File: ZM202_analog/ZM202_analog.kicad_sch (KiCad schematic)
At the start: 11 parts, among them U1 LM324, U13 LM393B, U14 LM358B

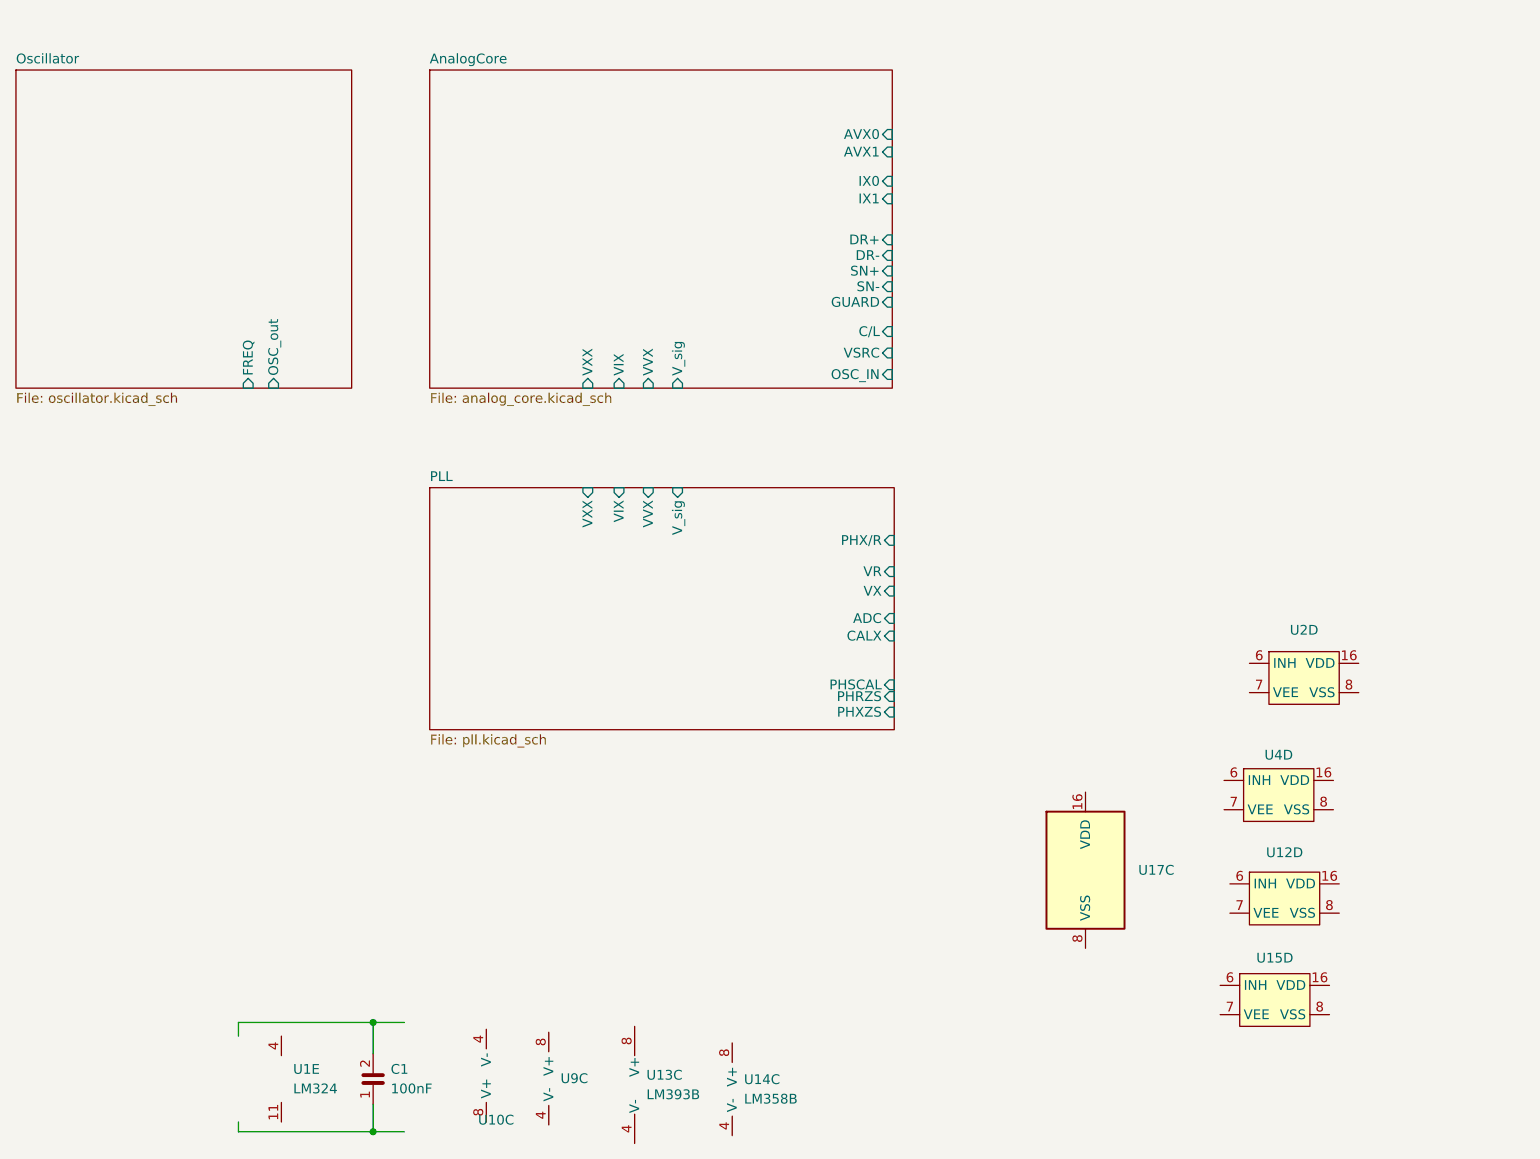
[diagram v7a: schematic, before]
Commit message: Connected hierarchical outlets to connector.
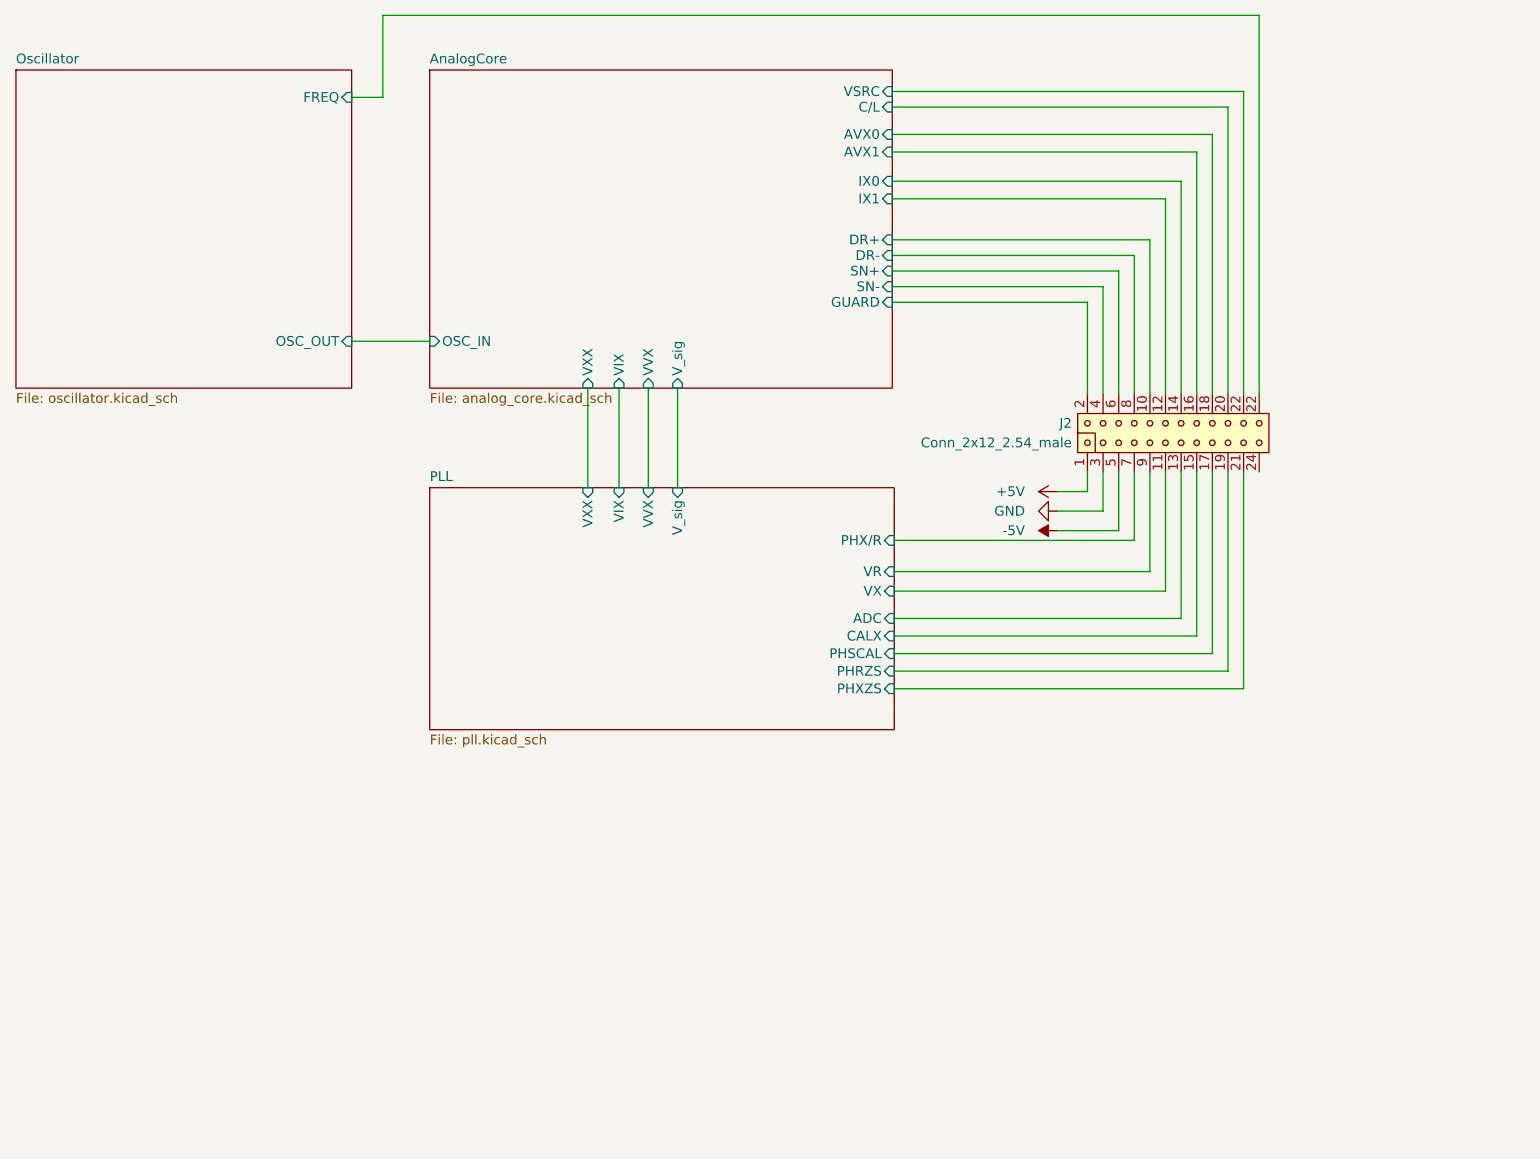
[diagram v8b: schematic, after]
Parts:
- removed C1: C0603_100nF_25V, Capacitor_SMD:C_0603_1608Metric, symbol Jojos_Lib:C0603_100nF_25V
- removed U1: LM324, Package_SO:SO-14_3.9x8.65mm_P1.27mm, symbol Jojos_Lib:LM324ADR
- removed U10, U9: ~, Package_SO:SO-8_3.9x4.9mm_P1.27mm, symbol Jojos_Lib:TLC2272CD
- removed U12, U15, U2, U4: ~, Package_SO:SOIC-16W_5.3x10.2mm_P1.27mm, symbol Jojos_Lib:CD4053
- removed U13: LM393B, Package_SO:SO-8_3.9x4.9mm_P1.27mm, symbol Jojos_Lib:LM393B
- removed U14: LM358B, Package_SO:SO-8_3.9x4.9mm_P1.27mm, symbol Jojos_Lib:LM358B
- removed U17: ~, Package_SO:SO-16_3.9x9.9mm_P1.27mm, symbol Jojos_Lib:CD4027BM96
- added J2: Conn_2x12_2.54_male, Connector_PinHeader_2.54mm:PinHeader_2x12_P2.54mm_Vertical, symbol Jojos_Lib:Conn_2x12_2.54_male
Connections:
- net AnalogCore/AVX0: now also J2.18
- net AnalogCore/AVX1: now also J2.16
- net AnalogCore/C/L: now also J2.20
- net AnalogCore/DR+: now also J2.10
- net AnalogCore/DR-: now also J2.8
- net AnalogCore/GUARD: now also J2.2
- net AnalogCore/IX0: now also J2.14
- net AnalogCore/IX1: now also J2.12
- net AnalogCore/SN+: now also J2.6
- net AnalogCore/SN-: now also J2.4
- net AnalogCore/VSRC: now also J2.22
- net Oscillator/FREQ: now also J2.22
- net PLL/ADC: now also J2.13
- net PLL/CALX: now also J2.15
- net PLL/PHRZS: now also J2.19
- net PLL/PHSCAL: now also J2.17
- net PLL/PHXZS: now also J2.21
- net PLL/PHX/R: now also J2.7
- net PLL/VR: now also J2.9
- net PLL/VX: now also J2.11
- new net +5V: J2.1
- new net -5V: J2.5
- new net GND: J2.3
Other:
- sheet Oscillator ports: added OSC_OUT; removed OSC_out
